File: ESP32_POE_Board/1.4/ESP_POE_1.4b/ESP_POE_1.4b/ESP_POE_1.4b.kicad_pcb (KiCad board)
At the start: 4 copper layers, 101.8 x 98.2 mm, 148 parts, among them J1 USB_C_Receptacle, J2 SI-46020-F, J3 HMTSW-102-X-X-S-X, J4 20021111-00012T4LF, J5 20021311-00012T4LF, J6 20021111-00012T4LF, J7 20021311-00012T4LF, Q1 Q12MHz/20pF/10ppm/4P/3.2x2.5mm, Q2 BC817-40(SOT23), Q3 BC817-40(SOT23)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

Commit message: updates
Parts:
- removed ACT1: LED/YELLOW/0603, OLIMEX_LEDs-FP:LED_0603_KA
- removed C10, C13, C19, C9: 22uF/6.3V/20%/X5R/C0603, OLIMEX_RLC-FP:C_0603_5MIL_DWS
- removed C11, C14, C15, C16, C18: 100nF/16V/10%/X7R/C0402, OLIMEX_RLC-FP:C_0402_5MIL_DWS
- removed C12, C24: 100nF/100V/10%/X7R/C0603, OLIMEX_RLC-FP:C_0603_5MIL_DWS
- removed C17: 2.2uF/6.3V/10%/X5R/C0603, OLIMEX_RLC-FP:C_0603_5MIL_DWS
- removed C2: 1nF/2000V/10%/X7R/C1206, OLIMEX_RLC-FP:C_1206_5MIL_DWS_ISO
- removed C20: NA(1.0nF/3kV/10%/X7R/SMD/1808(VISHAY-VJ1808Y102KBHAT4X_Farn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, OLIMEX_RLC-FP:C_1808(4520)_5MIL_DWS_ISO
- removed C21: NA(10uF/6.3V/20%/X5R/C0603), OLIMEX_RLC-FP:C_0603_5MIL_DWS
- removed C23: 1.0nF/3kV/10%/X7R/SMD/1808(VISHAY-VJ1808Y102KBHAT4X_Farnell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, OLIMEX_RLC-FP:C_1808(4520)_5MIL_DWS_ISO
- removed C25: 12pF/50V/5%/COG/C0402, OLIMEX_RLC-FP:C_0402_5MIL_DWS
- removed C26: 470uF/10V/20%/Low_ESR/RM2.5/6.0x11mm, OLIMEX_RLC-FP:CPOL-RM2.5mm_6.3x11mm_PTH
- removed C27: 15uF/100V/20%/RM2.5/6.3x11mm(Farnell:1281844), OLIMEX_RLC-FP:CPOL-RM2.5mm_6.3x11mm_PTH
- removed D10: SMAJ58A/SMA, OLIMEX_Diodes-FP:SMA-KA
- removed D5: SS510/100V/5A/0.85V/DO214AB(SMC), OLIMEX_Diodes-FP:DO214AB(SMC)_1(K)-2(A)
- removed D8: NA(SMBJ6.0A), OLIMEX_Diodes-FP:DO214AA_1(K)-2(A)
- removed DCDC1: F0505S-2WR2(SIP-7), OLIMEX_Regulators-FP:SIP-7_Universal
- removed Drill_Slot1, Drill_Slot3: 2 mm, OLIMEX_Other-FP:Mounting_hole_2_mm
- removed FET3: WPM2015-3/TR, OLIMEX_Transistors-FP:SOT23
- removed J2: SI-46020-F, SI-46020-F:BEL_SI-46020-F
- removed J3: HMTSW-102-X-X-S-X, HMTSW-102-X-X-S-X:SAMTEC_HMTSW-102-X-X-S-X
- removed J4, J6: 20021111-00012T4LF, 20021111-00012T4LF:CONN_20021111-XX012XXLF_AMP
- removed L1: FB0805/600R/2A, OLIMEX_RLC-FP:L_0805_5MIL_DWS
- removed L4: 33uH/2.1A/DCR=0.1R/20%/DBS135(PD3316MT330), OLIMEX_RLC-FP:DBS135
- removed LAN_CON1: RJP-003TC1(LPJ4112CNL), OLIMEX_Connectors-FP:RJP-003TC1(LPJ4112CNL)
- removed LNK1: LED/GREEN/0603, OLIMEX_LEDs-FP:LED_0603_KA
- removed Logo_OSHW: , OLIMEX_LOGOs-FP:LOGO_OPENHARDWARE_8x8
- removed Logo_Olimex: , OLIMEX_LOGOs-FP:OLIMEX_LOGO_TB
- removed R10, R11, R12, R13: 49.9R/1%/R0402, OLIMEX_RLC-FP:R_0402_5MIL_DWS
- removed R14, R15: 2.2k/R0402, OLIMEX_RLC-FP:R_0402_5MIL_DWS
- removed R2, R25, R44: 10k/R0402, OLIMEX_RLC-FP:R_0402_5MIL_DWS
- removed R22: 24.9k/1%/R0402, OLIMEX_RLC-FP:R_0402_5MIL_DWS
- removed R23: 180k/1%/R0402, OLIMEX_RLC-FP:R_0402_5MIL_DWS
- removed R26: 12.1k/1%/R0402, OLIMEX_RLC-FP:R_0402_5MIL_DWS
- removed R27: 4.42k/1%/1/16W/R0402, OLIMEX_RLC-FP:R_0402_5MIL_DWS
- removed R28: 0.03R/1%/R1206, OLIMEX_RLC-FP:R_1206_5MIL_DWS
- removed R3: 1k/R0402, OLIMEX_RLC-FP:R_0402_5MIL_DWS
- removed R33: 4.7R/R0402, OLIMEX_RLC-FP:R_0402_5MIL_DWS
- removed R34: 10.5k/1%/R0402, OLIMEX_RLC-FP:R_0402_5MIL_DWS
- removed R38: 56.2k/1%/R0402, OLIMEX_RLC-FP:R_0402_5MIL_DWS
- removed R41: 4.7k/R2512, OLIMEX_RLC-FP:R_2512_MM_DWS
- removed R43: 130k/R0402, OLIMEX_RLC-FP:R_0402_5MIL_DWS
- removed RM1, RM2: RA1206_(4X0603)_4B8_2.2k, OLIMEX_RLC-FP:R_MATRIX_4
- removed Sign_Antistatic: Val**, OLIMEX_LOGOs-FP:LOGO_ANTISTATIC_1
- removed Sign_CE: CE_Sign, OLIMEX_LOGOs-FP:CE_Sign
- removed Sign_PB-Free: , OLIMEX_LOGOs-FP:LOGO_PBFREE
- removed Sign_RecycleBin: , OLIMEX_LOGOs-FP:LOGO_RECYCLEBIN_1
- removed T1: LMUN2211LT1G(SOT-23), OLIMEX_Transistors-FP:SOT23
- removed TVS1: ESDS314DBVR(SOT-23-5), OLIMEX_Diodes-FP:SOT-23-5
- removed TVS2, TVS3: NA(GG0402052R542P), OLIMEX_Diodes-FP:D_0402_5MIL_DWS
- removed U2: TPS2376PW(TSSOP-8), OLIMEX_IC-FP:TSSOP-8_Pitch-0.65mm_Dimensions-4.40x3.00x1.20mm
- removed U4: LAN8710A-EZC(QFN32), OLIMEX_IC-FP:QFN32_EP(33)_5.00x5.00x0.90mm_Pitch_0.50mm
- removed U5: TX4138(ESOIC-8), OLIMEX_Regulators-FP:ESOIC-8
- moved J1 44.5 mm to (171.2, 163.8)
- moved MICRO_SD1 44.3 mm to (102.2, 62.4)
- moved R47 33.0 mm to (116.4, 61.8)
- moved U6 32.2 mm to (102.8, 67.3)
- moved FID5 23.6 mm to (117.1, 68.4)
- moved FID2 23.6 mm to (116.3, 68.4)
- moved FID1 22.5 mm to (88.5, 69.7)
- moved FID4 22.4 mm to (89.4, 69.7)
- moved L3 11.0 mm to (83.5, 159.3)
- moved L2 10.7 mm to (84.7, 133.4)
- moved BAT1 9.10 mm to (80.4, 183.7)
- moved R6 8.87 mm to (84.3, 172.5)
- moved R5 8.82 mm to (82.9, 172.5)
- moved C1 8.56 mm to (86.4, 173.1)
- moved PWR1 8.45 mm to (83.3, 169.5)
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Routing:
- net (no net): track 0.00 -> 1096.1 mm, vias 0 -> 70
- net /Shield: track 186.8 -> 0.00 mm, vias 17 -> 0
- net Earth: track 148.2 -> 0.00 mm, vias 21 -> 0
- net Spare1: track 120.8 -> 0.00 mm, vias 7 -> 0
- net Net-(D5-K): track 107.2 -> 0.00 mm, vias 8 -> 0
- net Net-(LAN_CON1-RCT): track 96.2 -> 0.00 mm, vias 6 -> 0
- net Spare2: track 79.0 -> 0.00 mm, vias 8 -> 0
- net /GPI34/BUT1: track 74.5 -> 0.00 mm, vias 5 -> 0
- net /D_Com: track 8.77 -> 83.2 mm, vias 0 -> 5
- net /RD-: track 60.8 -> 0.00 mm, vias 1 -> 0
- net /RD+: track 59.7 -> 0.00 mm, vias 2 -> 0
- net /ILIM: track 59.3 -> 0.00 mm, vias 5 -> 0
- net /TD-: track 55.8 -> 0.00 mm, vias 2 -> 0
- net /5V_DCDC: track 55.7 -> 0.00 mm, vias 1 -> 0
- net /TD+: track 54.3 -> 0.00 mm, vias 1 -> 0
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- added copper zone on B.Cu, net (none)
- added copper zone on F.Cu, net (none)
- added copper zone on In1.Cu, net (none)
- added copper zone on In2.Cu, net (none)
- removed copper zone on In2.Cu, net /ILIM
- removed copper zone on B.Cu, net /Shield
- removed copper zone on F.Cu, net /Shield
- removed copper zone on In1.Cu, net /Shield
- removed copper zone on In2.Cu, net /Shield
- removed copper zone on B.Cu, net Earth
- removed copper zone on F.Cu, net Earth
- removed copper zone on In1.Cu, net Earth
- removed copper zone on In1.Cu, net GND
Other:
- outline, holes or cut-outs redrawn

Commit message: updates
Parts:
- moved R5 80.0 mm to (63.7, 94.8)
- moved R6 80.0 mm to (65.2, 94.8)
- moved U3 80.0 mm to (67.2, 99.9)
- moved CHRG1 80.0 mm to (64.7, 98.1)
- moved FID3 80.0 mm to (64.8, 111.7)
- moved L2 80.0 mm to (65.5, 55.8)
- moved PWR1 80.0 mm to (64.1, 91.9)
- moved R8 80.0 mm to (64.7, 101.1)
- moved C1 80.0 mm to (67.3, 95.4)
- moved FID6 80.0 mm to (64.8, 111.8)
- moved L3 80.0 mm to (64.3, 81.7)
- moved BAT1 74.8 mm to (67.5, 110.0)
- moved R48 68.5 mm to (124.6, 35.4)
- moved R24 67.9 mm to (126.5, 42.9)
- moved Q3 67.5 mm to (128.1, 46.3)
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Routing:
- net /GPIO15/HS2_CMD: track 73.3 -> 0.00 mm, vias 5 -> 0
- net /GPIO14/HS2_CLK: track 57.9 -> 131.2 mm, vias 4 -> 9
- net /GPIO4/U1TXD: track 72.7 -> 125.3 mm, vias 6 -> 10
- net +3V3: track 156.4 -> 103.7 mm, vias 17 -> 13
- removed copper zone on In2.Cu, net +3V3
- removed copper zone on B.Cu, net GND
- removed copper zone on F.Cu, net GND

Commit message: POE2 layout
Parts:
- removed FID3, FID6: Fiducial, OLIMEX_Other-FP:Fiducial1x3
- removed MH1, MH2, MH3: Mounting_Hole_NPTH, OLIMEX_Other-FP:NPTH_2.2mm
- C29, C3, J5, L5, Q2, Q3, R20, R21, R31, R36, R39, R46: moved to F.Cu
- C4, C5, C6, C8, FET1, R18, R19, R29, R30, R32, R4, R47, R48, R9, U6, U7: moved to B.Cu
- moved FID5 134.4 mm to (92.5, 159.2)
- moved FID1 131.0 mm to (88.8, 159.2)
- moved R47 128.9 mm to (77.7, 156.6), turned to 180 degrees
- moved R48 128.6 mm to (77.7, 155.2)
- moved R24 121.8 mm to (76.3, 153.9), turned to 180 degrees
- moved D2 118.4 mm to (78.3, 152.5), turned to 90 degrees
- moved C29 109.7 mm to (75.8, 137.2), turned to 90 degrees
- moved MICRO_SD1 109.7 mm to (105.3, 144.1), turned to -90 degrees
- moved R42 108.8 mm to (79.2, 149.4), turned to 180 degrees
- moved U8 107.1 mm to (78.9, 137.3), turned to -90 degrees
- moved RM3 105.5 mm to (105.5, 152.3)
- moved R40 104.8 mm to (101.7, 149.8), turned to 0 degrees
- moved U6 104.4 mm to (90.4, 142.9), turned to 180 degrees
- moved R4 104.0 mm to (104.5, 136.0), turned to 180 degrees
- moved Q3 103.7 mm to (95.8, 144.9), turned to 0 degrees
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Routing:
- net (no net): track 1096.1 -> 0.00 mm, vias 70 -> 0
- net GND: track 356.8 -> 21.1 mm, vias 89 -> 7
- net /GPIO14/HS2_CLK: track 131.2 -> 0.00 mm, vias 9 -> 0
- net /GPIO4/U1TXD: track 125.3 -> 0.00 mm, vias 10 -> 0
- net +5V: track 116.1 -> 11.9 mm, vias 7 -> 0
- net /GPIO3/U0RXD: track 89.5 -> 0.00 mm, vias 3 -> 0
- net +3.3VLAN: track 88.0 -> 0.00 mm, vias 8 -> 0
- net /GPIO1/U0TXD: track 87.9 -> 0.00 mm, vias 3 -> 0
- net +3V3: track 103.7 -> 16.9 mm, vias 13 -> 6
- net Net-(U3-VBAT): track 94.5 -> 7.70 mm, vias 2 -> 1
- net /D_Com: track 83.2 -> 4.46 mm, vias 5 -> 0
- net /GPIO13/I2C-SDA: track 72.2 -> 0.00 mm, vias 3 -> 0
- net /GPIO2/HS2_DATA0: track 73.4 -> 2.93 mm, vias 4 -> 0
- net /GPIO16/I2C-SCL: track 76.4 -> 8.86 mm, vias 5 -> 0
- net /GPIO5/SPI_CS: track 67.0 -> 0.00 mm, vias 4 -> 0
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- added copper zone on In2.Cu, net +3V3
- added copper zone on In1.Cu, net GND
- removed copper zone on B.Cu, net (none)
- removed copper zone on F.Cu, net (none)
- removed copper zone on In1.Cu, net (none)
- removed copper zone on In2.Cu, net (none)
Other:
- board size 101.8 x 98.2 mm -> 40 x 40 mm
- copper layers 4 -> 6
- board text removed: "(C) 2022"
- board text removed: "+"
- board text removed: "+3V3"
- board text removed: "+5V"
- board text removed: "-"
- board text removed: "0"
- board text removed: "1"
- board text removed: "13"
- board text removed: "14"
- board text removed: "15"
- board text removed: "16"
- board text removed: "2"
- board text removed: "3"
- board text removed: "32"
- board text removed: "33"
- board text removed: "34"
- board text removed: "35"
- board text removed: "36"
- board text removed: "39"
- board text removed: "4"
- board text removed: "4 Layer PCB Dimensions: 28x98mm"
- board text removed: "5"
- board text removed: "9"
- board text removed: "Compliant"
- board text removed: "ESP32-PoE-ISO"
- board text removed: "ESP_EN"
- board text removed: "GND"
- board text removed: "Rev.K"
- board text removed: "RoHS"
- board text removed: "https://www.olimex.com"

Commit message: updates
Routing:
- net GND: track 21.1 -> 54.7 mm, vias 7 -> 10
- net Net-(MICRO_SD1-DAT1/RES): track 0.00 -> 14.9 mm
- net /GPIO12/PHY_PWR: track 0.00 -> 13.8 mm
- net /GPIO26/EMAC_RXD1(RMII): track 0.00 -> 10.3 mm
- net +3.3VLAN: track 0.00 -> 9.30 mm, vias 0 -> 1
- net /GPIO13/I2C-SDA: track 0.00 -> 7.79 mm
- net Net-(MICRO_SD1-CD/DAT3/CS): track 0.00 -> 7.78 mm
- net /GPIO27/EMAC_RX_CRS_DV: track 0.00 -> 7.38 mm
- net Net-(MICRO_SD1-DAT2/RES): track 0.00 -> 6.05 mm
- net Net-(U1-XO): track 6.77 -> 11.6 mm, vias 0 -> 1
- net Net-(U7-FB): track 0.00 -> 4.68 mm
- net /GPIO14/HS2_CLK: track 0.00 -> 2.18 mm

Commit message: updates
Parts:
- moved L2 27.9 mm to (82.2, 151.6)
- moved R40 0.77 mm to (100.9, 149.7), turned to 90 degrees
- moved R20 0.52 mm to (94.4, 137.8)
- moved R42 0.48 mm to (78.7, 149.2)
- turned R36 to -90 degrees
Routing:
- net /GPIO2/HS2_DATA0: track 2.93 -> 61.1 mm, vias 0 -> 3
- net /GPIO15/HS2_CMD: track 10.5 -> 54.5 mm, vias 0 -> 2
- net +5V: track 11.9 -> 52.8 mm, vias 0 -> 2
- net Net-(MICRO_SD1-VDD): track 2.24 -> 41.0 mm, vias 0 -> 2
- net Net-(U7-FB): track 4.68 -> 41.7 mm
- net Net-(U3-VBAT): track 7.70 -> 44.3 mm
- net /ESP_EN: track 6.78 -> 34.8 mm, vias 0 -> 4
- net /GPIO18/MDIO(RMII): track 0.00 -> 27.8 mm, vias 0 -> 1
- net /GPIO23/MDC(RMII): track 0.00 -> 26.5 mm, vias 0 -> 2
- net /GPIO13/I2C-SDA: track 7.79 -> 34.2 mm, vias 0 -> 1
- net Net-(MICRO_SD1-DAT0/DO): track 0.00 -> 25.5 mm, vias 0 -> 2
- net /GPIO33: track 0.00 -> 25.3 mm, vias 0 -> 1
- net Net-(R47-Pad2): track 1.42 -> 26.3 mm, vias 0 -> 2
- net /GPIO14/HS2_CLK: track 2.18 -> 25.7 mm, vias 0 -> 2
- net /GPI36/U1RXD: track 5.53 -> 28.8 mm, vias 0 -> 2
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
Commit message: fixing DRC
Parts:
- moved FID2 21.2 mm to (76.6, 132.3)
- moved FID5 9.27 mm to (83.4, 160.9)
- moved FID4 7.96 mm to (76.6, 132.3)
- moved FID1 5.77 mm to (83.3, 160.9)
- moved D7 2.70 mm to (83.4, 146.5), turned to 0 degrees
- moved C1 0.20 mm to (78.9, 151.1)
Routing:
- net /GPIO3/U0RXD: track 0.00 -> 48.8 mm, vias 0 -> 3
- net /+5V_USB: track 46.1 -> 90.3 mm, vias 1 -> 3
- net Net-(Q3-C): track 0.00 -> 24.8 mm, vias 0 -> 3
- net +5VP: track 28.2 -> 52.3 mm, vias 1 -> 3
- net Net-(D7-A): track 9.75 -> 31.6 mm, vias 0 -> 2
- net /GPI34/BUT1: track 0.00 -> 19.9 mm, vias 0 -> 2
- net /GPIO0: track 2.65 -> 20.4 mm, vias 0 -> 2
- net GND: track 72.1 -> 88.4 mm, vias 14 -> 18
- net /GPIO17/EMAC_CLK_OUT_180: track 0.00 -> 15.8 mm, vias 0 -> 2
- net /USB_D-: track 0.00 -> 13.3 mm, vias 0 -> 3
- net /USB_D+: track 0.00 -> 12.5 mm, vias 0 -> 3
- net /GPI35: track 7.69 -> 19.4 mm, vias 0 -> 2
- net +5V: track 52.8 -> 64.2 mm
- net Net-(Q3-E): track 6.98 -> 18.2 mm, vias 0 -> 2
- net /GPIO1/U0TXD: track 0.00 -> 10.7 mm, vias 0 -> 1
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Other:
- board text added: "- Cut off back 2 Through Hole connectors on USB-C so it does not poke ESP32 - B2B connectors are on the same side (even though they are on flipped sides)"

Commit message: POE 1 passes
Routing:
- net +5V: track 64.2 -> 82.5 mm, vias 2 -> 4
- net /GPIO25/EMAC_RXD0(RMII): track 42.7 -> 34.0 mm, vias 0 -> 1
- net /+5V_USB: track 90.3 -> 95.8 mm
- net GND: track 88.4 -> 88.9 mm, vias 18 -> 19

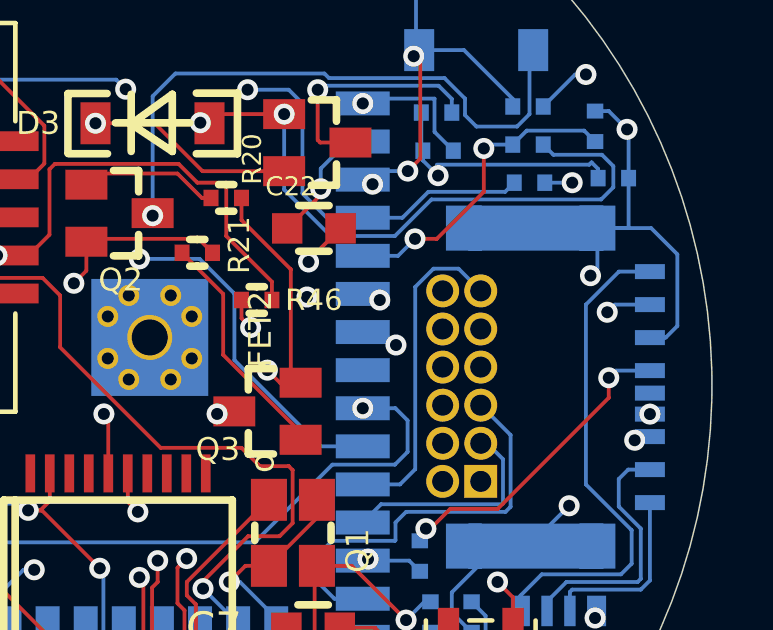
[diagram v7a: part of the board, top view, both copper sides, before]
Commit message: POE 2 passes DRC
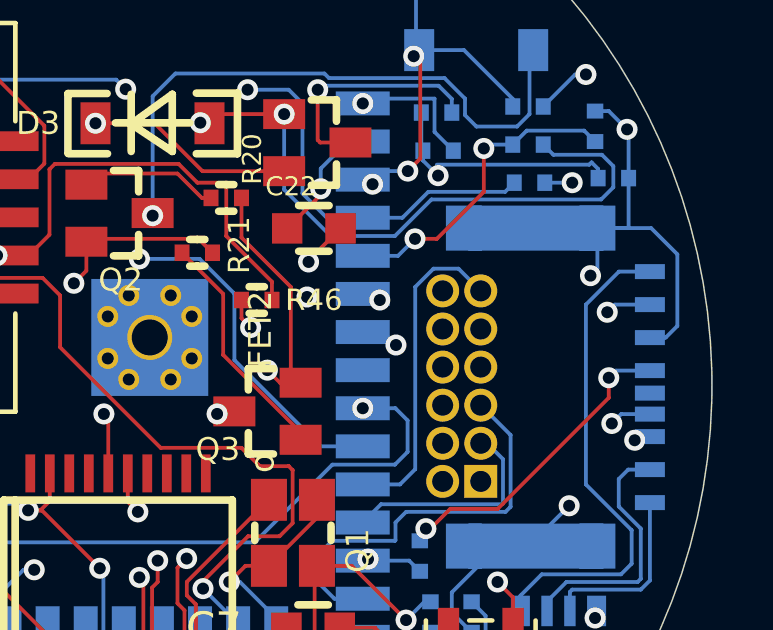
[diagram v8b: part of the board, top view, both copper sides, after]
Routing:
- net Net-(MICRO_SD1-VDD): track 41.0 -> 42.6 mm
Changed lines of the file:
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@@
   (segment (start 103.9876 134.7216) (end 103.9876 134.4676) (width 0.127) (layer "B.Cu") (net 6))
   (segment (start 79.6036 132.6388) (end 79.6036 134.874) (width 0.127) (layer "F.Cu") (net 7))
-  (via (at 108.5596 144.9756) (size 0.7) (drill 0.4) (layers "F.Cu" "B.Cu") (net 7))
+  (via (at 107.2896 145.288) (size 0.7) (drill 0.4) (layers "F.Cu" "B.Cu") (net 7))
   (via (at 79.6036 132.6388) (size 0.7) (drill 0.4) (layers "F.Cu" "B.Cu") (net 7))
-  (segment (start 107.7285 136.178883) (end 106.6292 135.079583) (width 0.127) (layer "In4.Cu") (net 7))
-  (segment (start 107.7285 144.1445) (end 107.7285 136.178883) (width 0.127) (layer "In4.Cu") (net 7))
-  (segment (start 108.5596 144.9756) (end 107.7285 144.1445) (width 0.127) (layer "In4.Cu") (net 7))
-  (segment (start 106.6292 134.9756) (end 105.2576 133.604) (width 0.127) (layer "In4.Cu") (net 7))
-  (segment (start 80.5688 133.604) (end 79.6036 132.6388) (width 0.127) (layer "In4.Cu") (net 7))
-  (segment (start 105.2576 133.604) (end 80.5688 133.604) (width 0.127) (layer "In4.Cu") (net 7))
-  (segment (start 106.6292 135.079583) (end 106.6292 134.9756) (width 0.127) (layer "In4.Cu") (net 7))
+  (segment (start 79.6036 132.6388) (end 80.5688 133.604) (width 0.127) (layer "In4.Cu") (net 7))
+  (segment (start 107.7285 136.178883) (end 107.7285 144.8491) (width 0.127) (layer "In4.Cu") (net 7))
+  (segment (start 107.7285 144.8491) (end 107.2896 145.288) (width 0.127) (layer "In4.Cu") (net 7))
+  (segment (start 106.6292 134.9756) (end 106.6292 135.079583) (width 0.127) (layer "In4.Cu") (net 7))
+  (segment (start 105.2576 133.604) (end 106.6292 134.9756) (width 0.127) (layer "In4.Cu") (net 7))
+  (segment (start 80.5688 133.604) (end 105.2576 133.604) (width 0.127) (layer "In4.Cu") (net 7))
+  (segment (start 106.6292 135.079583) (end 107.7285 136.178883) (width 0.127) (layer "In4.Cu") (net 7))
+  (segment (start 108.5596 144.9756) (end 107.602 144.9756) (width 0.127) (layer "B.Cu") (net 7))
+  (segment (start 107.602 144.9756) (end 107.2896 145.288) (width 0.127) (layer "B.Cu") (net 7))
   (segment (start 93.4024 153.384) (end 93.4212 153.3652) (width 0.127) (layer "F.Cu") (net 8))
   (segment (start 93.4584 153.3652) (end 93.1054 153.7182) (width 0.127) (layer "F.Cu") (net 8))
@@
   (segment (start 94.3356 143.002) (end 96.91624 145.58264) (width 0.127) (layer "F.Cu") (net 60))
   (segment (start 94.3356 140.97) (end 94.3356 143.002) (width 0.127) (layer "F.Cu") (net 60))
-  (segment (start 96.5891 143.60196) (end 96.91624 143.9291) (width 0.127) (layer "F.Cu") (net 61))
   (segment (start 91.1554 147.899) (end 91.4908 148.2344) (width 0.127) (layer "F.Cu") (net 61))
   (segment (start 96.2279 143.9291) (end 95.8088 143.51) (width 0.127) (layer "F.Cu") (net 61))
-  (segment (start 94.9452 137.7696) (end 94.9452 138.5062) (width 0.127) (layer "F.Cu") (net 61))
-  (segment (start 94.9452 138.5062) (end 96.5891 140.1501) (width 0.127) (layer "F.Cu") (net 61))
+  (segment (start 96.5891 143.60196) (end 96.91624 143.9291) (width 0.127) (layer "F.Cu") (net 61))
+  (segment (start 94.9452 137.7696) (end 94.9452 139.0904) (width 0.127) (layer "F.Cu") (net 61))
   (segment (start 96.91624 143.9291) (end 96.2279 143.9291) (width 0.127) (layer "F.Cu") (net 61))
-  (segment (start 96.5891 140.1501) (end 96.5891 143.60196) (width 0.127) (layer "F.Cu") (net 61))
+  (segment (start 96.5891 140.7343) (end 96.5891 143.60196) (width 0.127) (layer "F.Cu") (net 61))
   (segment (start 91.1554 146.9517) (end 91.1554 147.899) (width 0.127) (layer "F.Cu") (net 61))
+  (segment (start 94.9452 139.0904) (end 96.5891 140.7343) (width 0.127) (layer "F.Cu") (net 61))
   (via (at 95.8088 143.51) (size 0.7) (drill 0.4) (layers "F.Cu" "B.Cu") (net 61))
   (via (at 91.4908 148.2344) (size 0.7) (drill 0.4) (layers "F.Cu" "B.Cu") (net 61))
@@
   (via (at 99.163106 149.809029) (size 0.7) (drill 0.4) (layers "F.Cu" "B.Cu") (net 69))
   (via (at 83.6676 141.1224) (size 0.7) (drill 0.4) (layers "F.Cu" "B.Cu") (net 69))
-  (segment (start 82.7903 145.1727) (end 83.1271 145.5095) (width 0.127) (layer "In4.Cu") (net 69))
   (segment (start 82.7903 141.9997) (end 82.7903 145.1727) (width 0.127) (layer "In4.Cu") (net 69))
-  (segment (start 83.1271 145.5095) (end 94.863577 145.5095) (width 0.127) (layer "In4.Cu") (net 69))
-  (segment (start 94.863577 145.5095) (end 99.163106 149.809029) (width 0.127) (layer "In4.Cu") (net 69))
   (segment (start 83.6676 141.1224) (end 82.7903 141.9997) (width 0.127) (layer "In4.Cu") (net 69))
+  (segment (start 82.7903 145.1727) (end 83.234609 145.617009) (width 0.127) (layer "In4.Cu") (net 69))
+  (segment (start 95.099277 145.7452) (end 99.163106 149.809029) (width 0.127) (layer "In4.Cu") (net 69))
+  (segment (start 83.789883 145.5095) (end 84.025583 145.7452) (width 0.127) (layer "In4.Cu") (net 69))
+  (segment (start 83.342117 145.5095) (end 83.789883 145.5095) (width 0.127) (layer "In4.Cu") (net 69))
+  (segment (start 83.234609 145.617009) (end 83.342117 145.5095) (width 0.127) (layer "In4.Cu") (net 69))
+  (segment (start 84.025583 145.7452) (end 95.099277 145.7452) (width 0.127) (layer "In4.Cu") (net 69))
   (segment (start 100.5332 149.86) (end 100.8888 150.2156) (width 0.127) (layer "B.Cu") (net 69))
   (segment (start 98.988 149.86) (end 100.5332 149.86) (width 0.127) (layer "B.Cu") (net 69))
